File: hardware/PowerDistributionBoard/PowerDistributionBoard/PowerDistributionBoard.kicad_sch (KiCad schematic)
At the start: 95 parts, among them J1 Battery, J10 ESC2_PWR, J2 FAN 1, J3 FAN 2, J4 FAN 3, J5 FAN 4, J6 Inverter, J7 Control Board, J8 Conn_01x02, J9 ESC1_PWR, K1 J115F11AH12VDCS61.5, K2 J115F11AH12VDCS61.5, Q1 Q_NMOS_GDS, Q2 Q_NPN_EBC, Q3 Q_NMOS_GSD, Q4 Q_NMOS_GSD, Q5 Q_NPN_EBC, Q6 Q_NMOS_GSD, Q7 Q_NMOS_GSD, Q8 Q_NPN_BEC, SW1 SW_SPDT, U1 LT1641-1, U2 MAX6643LBBAEET, U3 MAX6643LBBAEET, U4 MC74HC20ADG, U5 KSTW004A2B41Z, U6 AP2210N-3.3TRG1

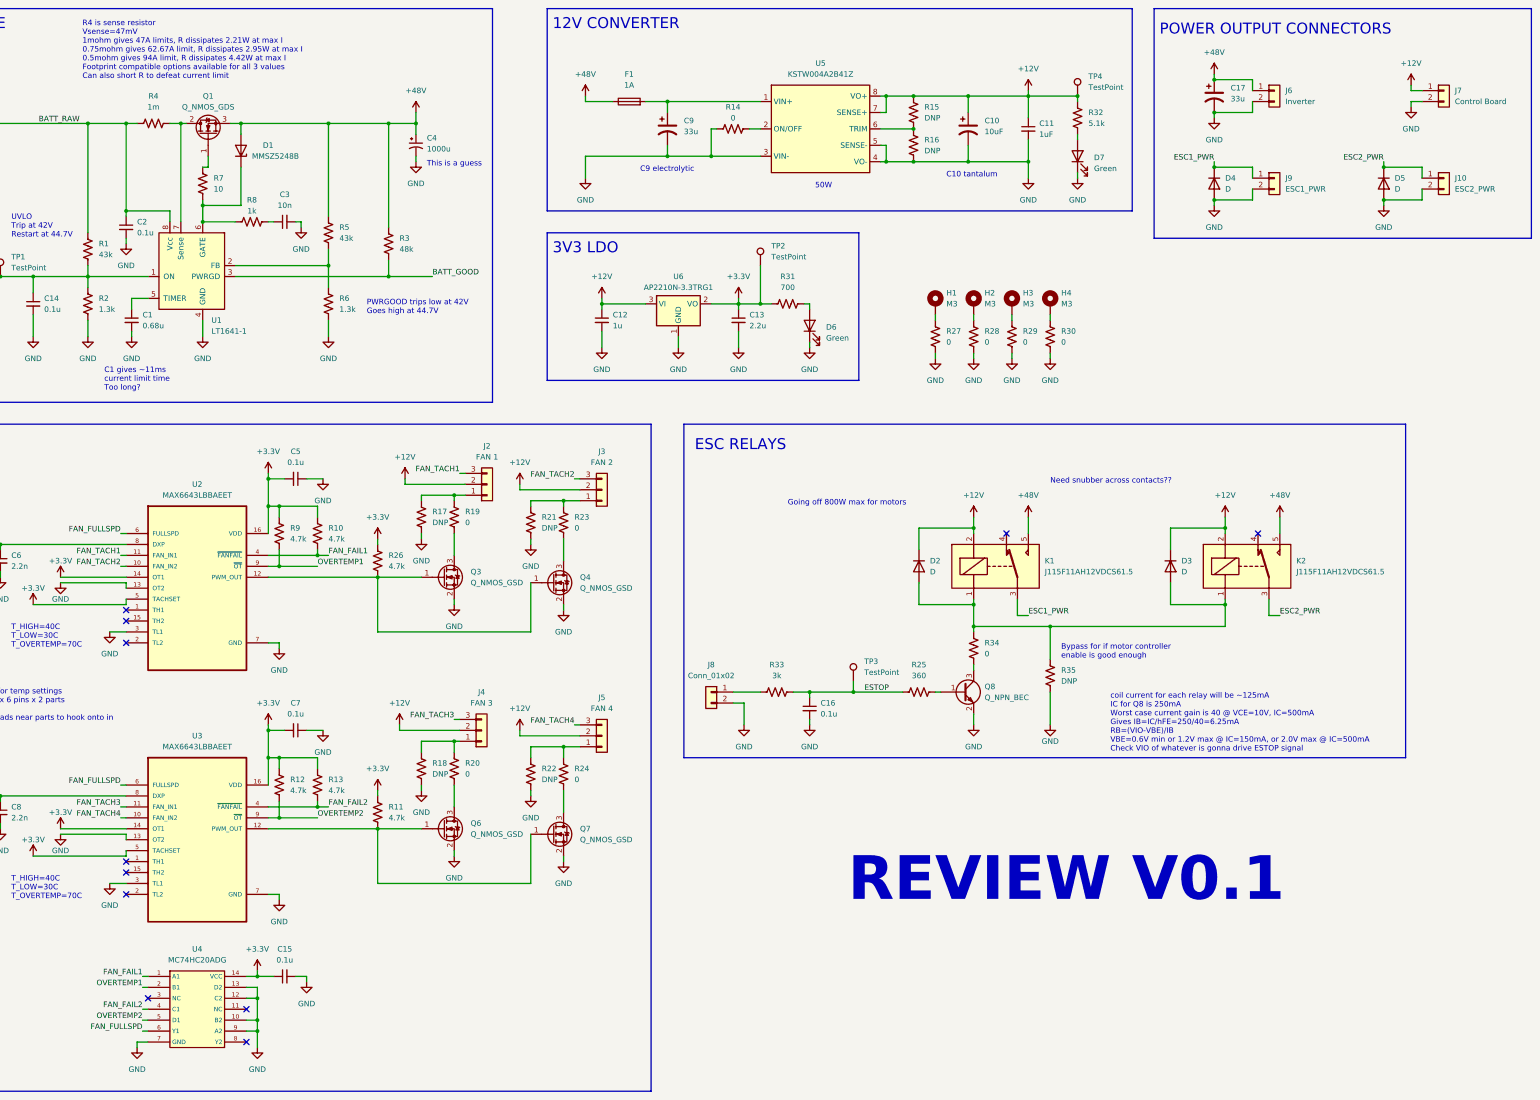
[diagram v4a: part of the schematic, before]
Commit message: PDB schematic - Add router power, address review comments
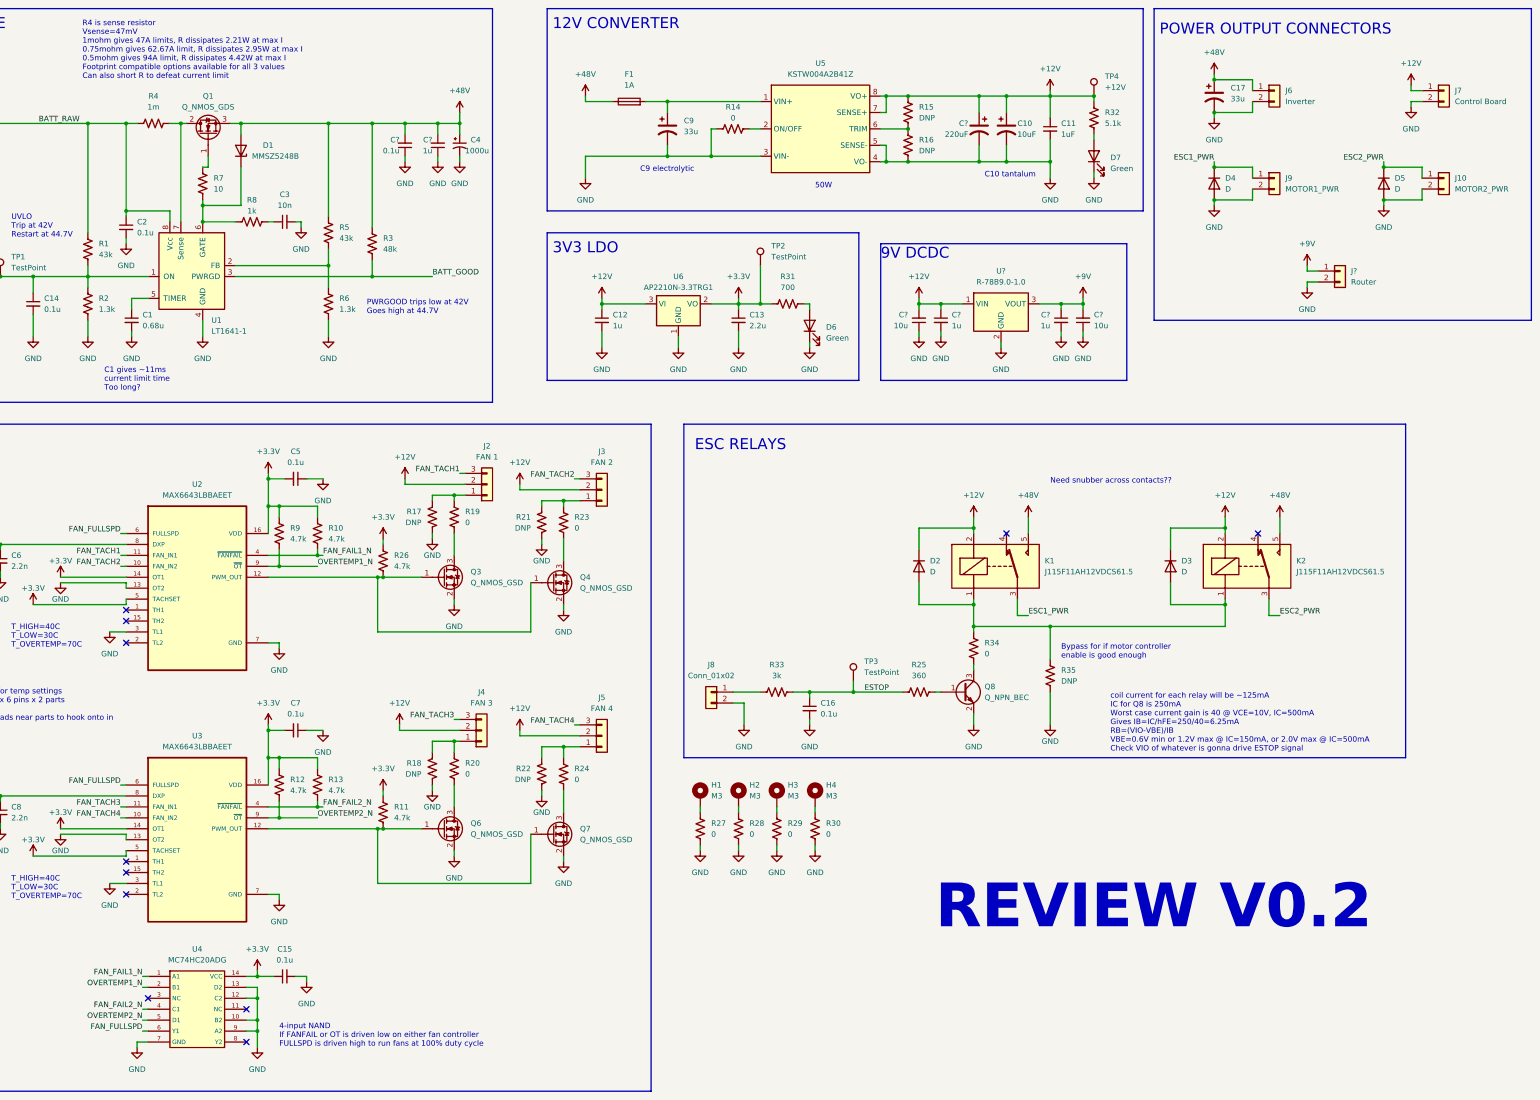
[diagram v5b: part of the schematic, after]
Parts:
- added C?: 220uF, Capacitor_THT:CP_Radial_D6.3mm_P2.50mm, symbol Device:C_Polarized_US
- added C? (x3): 1u, Capacitor_SMD:C_0805_2012Metric, symbol Device:C_Small
- added C?: 0.1u, Capacitor_SMD:C_0805_2012Metric, symbol Device:C_Small
- added C? (x2): 10u, Capacitor_SMD:C_0805_2012Metric, symbol Device:C_Small
- added J?: Router, Connector_Molex:Molex_Micro-Fit_3.0_43650-0200_1x02_P3.00mm_Horizontal, symbol Connector_Generic:Conn_01x02
- added U?: R-78B9.0-1.0, PDBLib:R-78B9.0-1.0, symbol PBD_LIB:R-78B9.0-1.0
- J10: value ESC2_PWR -> MOTOR2_PWR
- J9: value ESC1_PWR -> MOTOR1_PWR
- TP4: value TestPoint -> +12V
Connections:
- net +12V: now also C?.1, C?.1, C?.2, U?.1 (VIN)
- net +48V: now also C?.2, C?.2
- net GND: now also R17.1, R18.1, R21.1, R22.1, C?.1, C?.1, C?.1, C?.1, C?.2, C?.2, C?.2, J?.2 (Pin_2), U?.2 (GND); no longer R17.2, R18.2, R21.2, R22.2
- net at J3.1 (Pin_1), R23.1: now also R21.2; no longer R21.1
- net at J2.1 (Pin_1), R19.1: now also R17.2; no longer R17.1
- net at J4.1 (Pin_1), R20.1: now also R18.2; no longer R18.1
- net at J5.1 (Pin_1), R24.1: now also R22.2; no longer R22.1
- net FAN_FAIL1 renamed FAN_FAIL1_N
- net FAN_FAIL2 renamed FAN_FAIL2_N
- net OVERTEMP1 renamed OVERTEMP1_N
- net OVERTEMP2 renamed OVERTEMP2_N
- new net +9V: C?.1, C?.2, J?.1 (Pin_1), U?.3 (VOUT)
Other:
- note added: "4-input NAND If FANFAIL or OT is driven low on either fan controller FULLSPD is driven high to run fans at 100% duty cycle"
- note added: "9V DCDC"
- note added: "REVIEW V0.2"
- note removed: "Going off 800W max for motors"
- note removed: "REVIEW V0.1"
- note removed: "This is a guess"
- moved on the sheet: C10, C11, C4, D7, H1, H2, H3, H4, R11, R15, R16, R17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

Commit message: Replace Relays with FETs for Motor Power Switching
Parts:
- removed C16: 0.1u, Capacitor_SMD:C_0805_2012Metric, symbol Device:C_Small
- removed D2, D3: D, Diode_SMD:D_SMA, symbol Device:D
- removed D4, D5: D, Package_TO_SOT_THT:TO-247-2_Horizontal_TabDown, symbol Device:D
- removed J8: Conn_01x02, Connector_Molex:Molex_Micro-Fit_3.0_43650-0215_1x02_P3.00mm_Vertical, symbol Connector_Generic:Conn_01x02
- removed K1, K2: J115F11AH12VDCS61.5, PDBLib:J115F11AH12VDCS61.5, symbol PBD_LIB:J115F11AH12VDCS61.5
- removed Q8: Q_NPN_BEC, Package_TO_SOT_SMD:SOT-23, symbol Device:Q_NPN_BEC
- removed R25: 360, Resistor_SMD:R_0805_2012Metric, symbol Device:R_US
- removed R33: 3k, Resistor_SMD:R_0805_2012Metric, symbol Device:R_US
- removed R34: 0, Resistor_SMD:R_0805_2012Metric, symbol Device:R_US
- removed R35: DNP, Resistor_SMD:R_0805_2012Metric, symbol Device:R_US
- removed TP3: TestPoint, TestPoint:TestPoint_Pad_D1.0mm, symbol Connector:TestPoint
- added D? (x2): D, Package_TO_SOT_THT:TO-247-2_Horizontal_TabDown, symbol Device:D
- added J?: Conn_01x02, Connector_Molex:Molex_Micro-Fit_3.0_43650-0215_1x02_P3.00mm_Vertical, symbol Connector_Generic:Conn_01x02
- added Q? (x2): TK100E10N1,S1X, Package_TO_SOT_THT:TO-220-3_Vertical, symbol Device:Q_NMOS_GDS
- added Q?: DMN62D0U-13, PDBLib:DMN62D0U-13, symbol Device:Q_NMOS_GSD
- added R?: 330, Resistor_SMD:R_0805_2012Metric, symbol Device:R_US
- added R? (x4): 1k, Resistor_SMD:R_0805_2012Metric, symbol Device:R_US
- added R? (x4): 0, symbol Device:R_US
- added TP?: ESTOP, TestPoint:TestPoint_Pad_D1.0mm, symbol Connector:TestPoint
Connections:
- net ESC1_PWR is gone; now on net +48V: J9.1 (Pin_1)
- net ESC2_PWR is gone; now on net +48V: J10.1 (Pin_1)
- net +12V: now also R?.2
- net +48V: now also D?.1 (K), D?.1 (K)
- net ESTOP: now also J?.1 (Pin_1), R?.1, R?.2, TP?.1
- net GND: now also J?.2 (Pin_2), Q?.2 (S), Q?.3 (S), Q?.3 (S), R?.2, R?.2; no longer J10.2 (Pin_2), J9.2 (Pin_2)
- new net: Q?.1 (G), R?.1
- new net: D?.2 (A), J10.2 (Pin_2), R?.1, R?.2
- new net: Q?.1 (G), R?.2 (x2)
- new net: Q?.2 (D), R?.1 (x2)
- new net: D?.2 (A), J9.2 (Pin_2), R?.1, R?.2
- new net +3V3: R?.2
- new net MOTOR_FET_GATE: Q?.3 (D), R?.1, R?.1, R?.1
- no-connect marks 12 -> 10
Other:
- note added: "0 ohm here because easier to depop than FET"
- note added: "ESTOP is signal from 74LVC1G97W6-7 logic IC on control board 3.3V output, can sink max 24mA Say we want IC on control board to sink 10mA Rgate = 3.3V/10mA = 330Ω Check current of motor driver EN signals on control board"
- note added: "FET to control motor power fets from ESTOP signals If ESTOP active (high), this FET is on and gates of motor power FETs are pulled low, cutting motor power If ESTOP not active (low), this fet is off and gates of motor power FETs are on, enabling motor power Want 3.3V pull up to keep motor power off by default, but could the ESTOP signal cause issues with the LDO if ESTOP_H > 3V3 on this board? Us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"
- note added: "MOTOR POWER"
- note added: "MOTOR_FET_GATE net is pulled up (12V, 1k) Rgate to soften current discharge through other FET when gate pulled to ground I = 12V/1k = 12mA"
- note added: "Motor continuous current is 6A Max Rds given as 3.4mΩ at 25C ambient Fig 8.6 in datasheet gives ~3.7mΩ at 70C ambient so not bad Pd = 6^2 * 3.7e-3 = 0.1332W Tch(max) = 150C Using given Rth(ch-amb)=83.3C/W, Trise = 83.3 * 0.1332 = 11.096C 577102B00000G heatsink has Rth = 25.90C/W with no airflow With heatsink, Rth(ch-amb)=Rth(ch-c)+Rth(c-amb)=0.49+25.90=26.39C/W This gives Trise = 26.39 * 0.1332 =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"
- note added: "REVIEW V0.1"
- note removed: "Bypass for if motor controller enable is good enough"
- note removed: "ESC RELAYS"
- note removed: "Need snubber across contacts??"
- note removed: "REVIEW V0.2"
- note removed: "coil current for each relay will be ~125mA IC for Q8 is 250mA Worst case current gain is 40 @ VCE=10V, IC=500mA Gives IB=IC/hFE=250/40=6.25mA RB=(VIO-VBE)/IB VBE=0.6V min or 1.2V max @ IC=150mA, or 2.0V max @ IC=500mA Check VIO of whatever is gonna drive ESTOP signal"
- moved on the sheet: H1, H2, H3, H4, J?, R27, R28, R29, R30

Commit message: Power Board Changes
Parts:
- added D2: SML-P11UTT86R, LED_SMD:LED_0402_1005Metric, symbol Device:LED
- added D3, D4, D5, D8: S1G, Diode_SMD:D_SMA, symbol Device:D_Small
- added R25: 3.4k, Resistor_SMD:R_0805_2012Metric, symbol Device:R_US
- added R? (x2): 100, Resistor_SMD:R_0805_2012Metric, symbol Device:R_US
- R17, R18, R21, R22: value DNP -> 0; DNP (none) -> DNP
- R3: value 48k -> 46.4k
- TP1: value TestPoint -> ON
- gave numbers to parts that had none: 25
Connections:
- net +12V: now also D3.1 (K), D4.1 (K), D5.1 (K), D8.1 (K)
- net +48V: now also R?.2; no longer D1.2 (A)
- net BATT_GOOD: now also D2.2 (A), R25.1; no longer U1.3 (PWRGD)
- net GND: now also R25.2
- net at C14.1, R1.2, R2.1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: now also R?.1; no longer SW1.3 (C)
- net at J3.1 (Pin_1), R21.2, R23.1: now also D5.2 (A)
- net at J2.1 (Pin_1), R17.2, R19.1: now also D4.2 (A)
- net at J4.1 (Pin_1), R18.2, R20.1: now also D3.2 (A)
- net at J5.1 (Pin_1), R22.2, R24.1: now also D8.2 (A)
- new net: R?.2, SW1.3 (C)
- new net: D1.2 (A), R?.1
- new net: D2.1 (K), U1.3 (PWRGD)
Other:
- note added: "If BATT_GOOD signal is needed remove D2 and populate R25 to get 3.3V signal"
- moved on the sheet: D1, Q4, Q7, R21, R22, R23, R24, R7, SW1, TP1

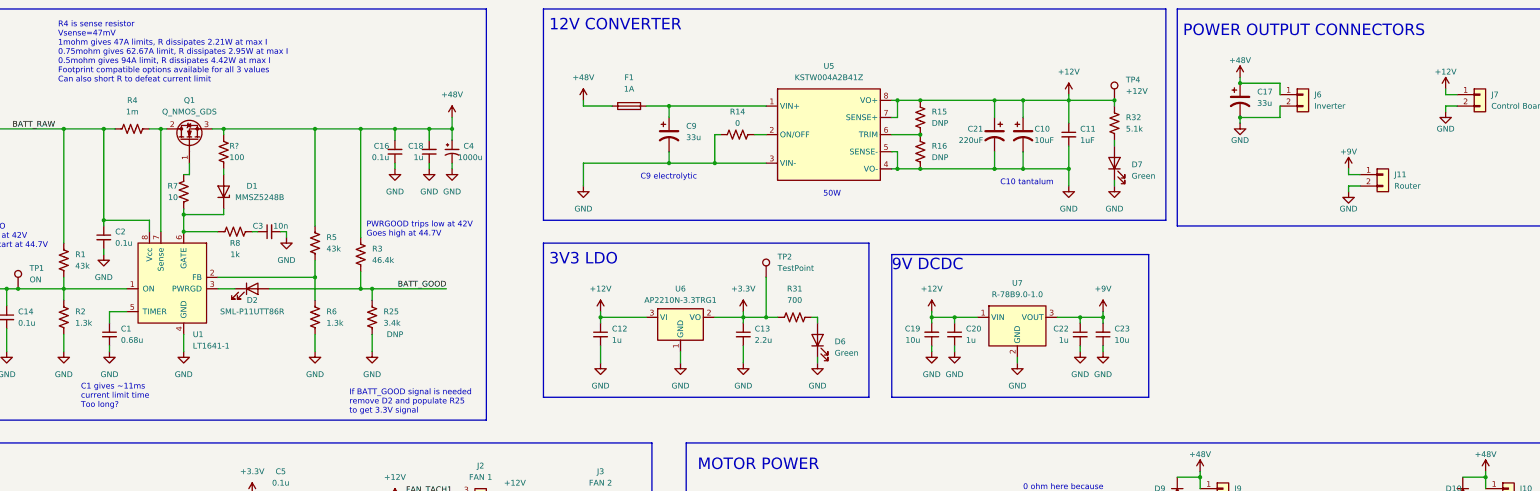
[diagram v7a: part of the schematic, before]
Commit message: PDB Hot Swap Circuit Changes/Review, Add Flybacks
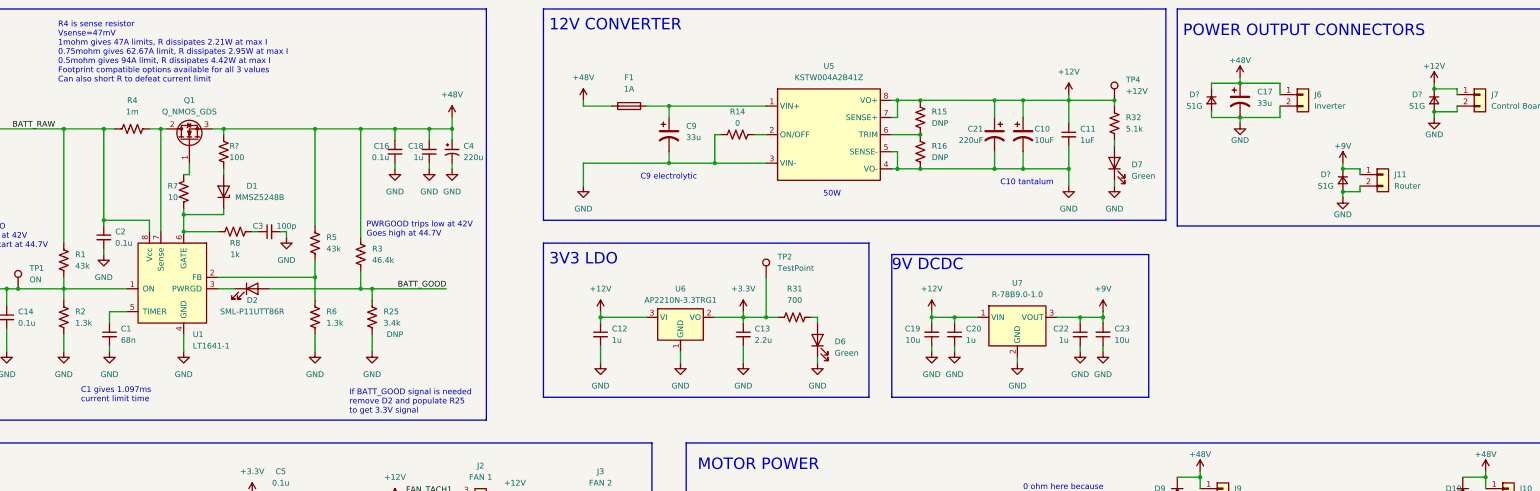
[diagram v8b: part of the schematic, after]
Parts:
- added D? (x3): S1G, Diode_SMD:D_SMA, symbol Device:D_Small
- C1: value 0.68u -> 68n
- C3: value 10n -> 100p
- C4: value 1000u -> 220u; footprint Capacitor_THT:CP_Radial_D18.0mm_P7.50mm -> Capacitor_THT:CP_Radial_D16.0mm_P7.50mm; Digikey 493-1152-ND -> 493-5867-ND; LCSC (none) -> C1580233; Voltage (none) -> 48V
- R37, R38, R40, R41: footprint (none) -> Resistor_SMD:R_2512_6332Metric; Digikey (none) -> HCJ2512ZT0R00CT-ND; LCSC (none) -> C346503
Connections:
- net +12V: now also D?.1 (K)
- net +48V: now also D?.1 (K)
- net +9V: now also D?.1 (K)
- net GND: now also D?.2 (A), D?.2 (A), D?.2 (A)
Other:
- note added: "C1 gives 1.097ms current limit time"
- note removed: "C1 gives ~11ms current limit time Too long?"
